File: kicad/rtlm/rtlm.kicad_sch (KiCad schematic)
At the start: 265 parts, among them IC1 ESP32-S3FN8, IC2 TPS25940ARVCR, IC3 PE4259, IC4 TPS2553DBVR, IC5 TLV9004IDR, IC6 TLV9004IDR, IC7 TCAN1042HGVDR, IC8 TPS2553DBVR, IC9 TLC59116IPWR, J1 USB_C_Receptacle_USB2.0_16P, J10 TEMP_2, J11 TEMP_3, J12 TEMP_4, J13 ANALOG_1, J14 ANALOG_2, J15 ANALOG_3, J16 ANALOG_4, J17 DM3AT-SF-PEJM5, J18 CAN_EXPANSION, J19 BATTERY_VOLTAGE_SENSE_LINE, J2 Conn_01x02, J3 UART_DEBUG_3V3, J4 LORA_ANT, J5 PULSE_1, J6 PULSE_2, J7 PULSE_3, J8 PULSE_4, J9 TEMP_1, Q1 DMP2035U-7, SW1 SW_Push, SW2 SW_Push, U1 TPS62130A, U10 RV-3028-C7, U2 TPS2116DRL, U3 TPD2EUSB30, U4 SX1262IMLTRT, U5 SN74LVC14ADR, U6 MCP3208-BI/SL, U7 REF3025AIDBZR, U8 AMC3330, U9 ADS1115IDGS, Y1 40MHz, Y2 TG2520SMN 32.0000M-MCGNNM3

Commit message: Separate USB programming power and protect the pack divider
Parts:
- added D35: BAS70-04, Package_TO_SOT_SMD:SOT-23, symbol Device:D_Schottky_Dual_Series_AKC
- added R95: 16.4k, Resistor_SMD:R_0603_1608Metric, symbol Device:R
- C4: value 3.3nf -> 22nF; MPN CC0603KRX7R9BB332 -> CC0603KRX7R9BB223; Selection Notes Specified MLCC value/package; manufacturer datasheet and DC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 -> Slower MCU-only buck soft start for USB programming inrush;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
- R84: value 8.2k -> 16.4k; MPN TNPW06038K20BEEA -> TNPW060316K4BEEA
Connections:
- net +3.3V: no longer C10.2, C11.2, C14.2, C15.2, C16.1, C3.1, IC1.20 (VDD3P3_RTC), IC1.46 (VDD3P3_CPU), IC1.55 (VDDA_1), IC1.56 (VDDA_2), L1.2, L2.1, R16.2, R17.2, R6.2, U1.14 (VOS)
- net HLDO_OUT: now also D35.2 (K)
- net PACK_NEG: now also D35.1 (A), R95.1
- net PACK_V_SENSE: now also D35.3 (common)
- net PACK_DIVIDED: now reaches C74.1, R83.2, R84.2, R90.1
- net PACK_DIVIDED: now also R95.2
- net MUX_EXT_SELECTED: now reaches R8.1, U2.8 (ST)
- new net +3V3_MCU: C10.2, C11.2, C14.2, C15.2, C16.1, C3.1, IC1.20 (VDD3P3_RTC), IC1.46 (VDD3P3_CPU), IC1.55 (VDDA_1), IC1.56 (VDDA_2), L1.2, L2.1, R16.2, R17.2, R6.2, U1.14 (VOS)
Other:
- added sheet USB service power (service_power.kicad_sch)
- note added: "R84 || R95 = 8.2k. One leg open at96V: INP <1.56V. D35: isolated-rail clamps."

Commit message: Move USB service-power circuit into the main schematic
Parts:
- added C82, C85, C88, C89: 100nF, Capacitor_SMD:C_0603_1608Metric, symbol Device:C
- added C83: 1uF, Capacitor_SMD:C_0603_1608Metric, symbol Device:C
- added C84: 1nF, Capacitor_SMD:C_0603_1608Metric, symbol Device:C
- added C86: 130pF, Capacitor_SMD:C_0603_1608Metric, symbol Device:C
- added C87: 220nF, Capacitor_SMD:C_0603_1608Metric, symbol Device:C
- added C90: 10nF, Capacitor_SMD:C_0603_1608Metric, symbol Device:C
- added Q2, Q3: MMBT3904-7-F, Package_TO_SOT_SMD:SOT-23, symbol Transistor_BJT:Q_NPN_BEC
- added R100: 100, Resistor_SMD:R_0603_1608Metric, symbol Device:R
- added R101, R103, R98: 10k, Resistor_SMD:R_0603_1608Metric, symbol Device:R
- added R102, R104, R105, R96: 100k, Resistor_SMD:R_0603_1608Metric, symbol Device:R
- added R97: 1M, Resistor_SMD:R_0603_1608Metric, symbol Device:R
- added R99: 47k, Resistor_SMD:R_0603_1608Metric, symbol Device:R
- added U11: TPS22917DBVR, Package_TO_SOT_SMD:SOT-23-6, symbol Power_Management:TPS22917DBV
- added U12: TPS3808G01DBVR, Package_TO_SOT_SMD:SOT-23-6, symbol Power_Supervisor:TPS3808DBV
- added U13: SN74LVC1G17DBVR, Package_TO_SOT_SMD:SOT-23-5, symbol 74xGxx:74LVC1G17
- added U14: SN74LVC2G86DCTR, Package_SO:SSOP-8_2.95x2.8mm_P0.65mm, symbol 74xGxx:74LVC2G86
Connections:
- net +3.3V: now also C83.1, R100.1, U11.6 (VOUT)
- net +3V3_MCU: now also C82.1, C84.2, C85.1, C88.1, C89.1, R98.1, U11.1 (VIN), U12.3 (~{MR}), U12.6 (VDD), U13.5 (VCC), U14.6, U14.8 (VCC)
- net ESP_BOOT: now also Q3.3 (C)
- net ESP_RESET: now also Q2.3 (C)
- net GND: now also C82.2, C83.2, C85.2, C86.2, C87.2, C88.2, C89.2, C90.2, Q2.2 (E), Q3.2 (E), R102.2, R104.2, R105.2, R97.2, U11.2 (GND), U12.2 (GND), U13.3 (GND), U14.4 (GND)
- net MUX_EXT_SELECTED: now also R96.1
- new net BOOT_BASE: Q3.1 (B), R103.2, R104.1
- new net EXT_SENSE: C90.1, R96.2, R97.1, U12.5 (SENSE)
- new net EXT_VALID: R98.2, R99.1, U12.1 (~{RESET}), U14.1, U14.5
- new net MODE_EDGE: R101.1, U14.7
- new net PERIPH_ENABLE: R105.1, U11.3 (ON), U13.4, U14.2
- new net PERIPH_QOD: R100.2, U11.5 (QOD)
- new net RESET_BASE: Q2.1 (B), R101.2, R102.1
- new net SERVICE_DELAY: C87.1, R99.2, U13.2
- new net SUPERVISOR_CT: C86.1, U12.4 (CT)
- new net SWITCH_CT: C84.1, U11.4 (CT)
- new net USB_SERVICE: R103.1, U14.3
- no-connect marks 44 -> 45
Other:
- removed sheet USB service power
- note added: "Automatic USB programming service mode"
- note added: "TPS22917 CT -> VIN. Reset pulse = raw flag XOR Schmitt-delayed flag. Q2/Q3 are open collector; manual BOOT and RESET remain usable. Do not disable ROM USB download with security eFuses if USB service is required."
- note added: "USB only: peripherals OFF; GPIO0 forced LOW; ESP boots ROM download. Mux confirms external5V selected: peripherals ramp ON; ESP resets and boots application. Either power-mode transition resets ESP before peripheral power changes."

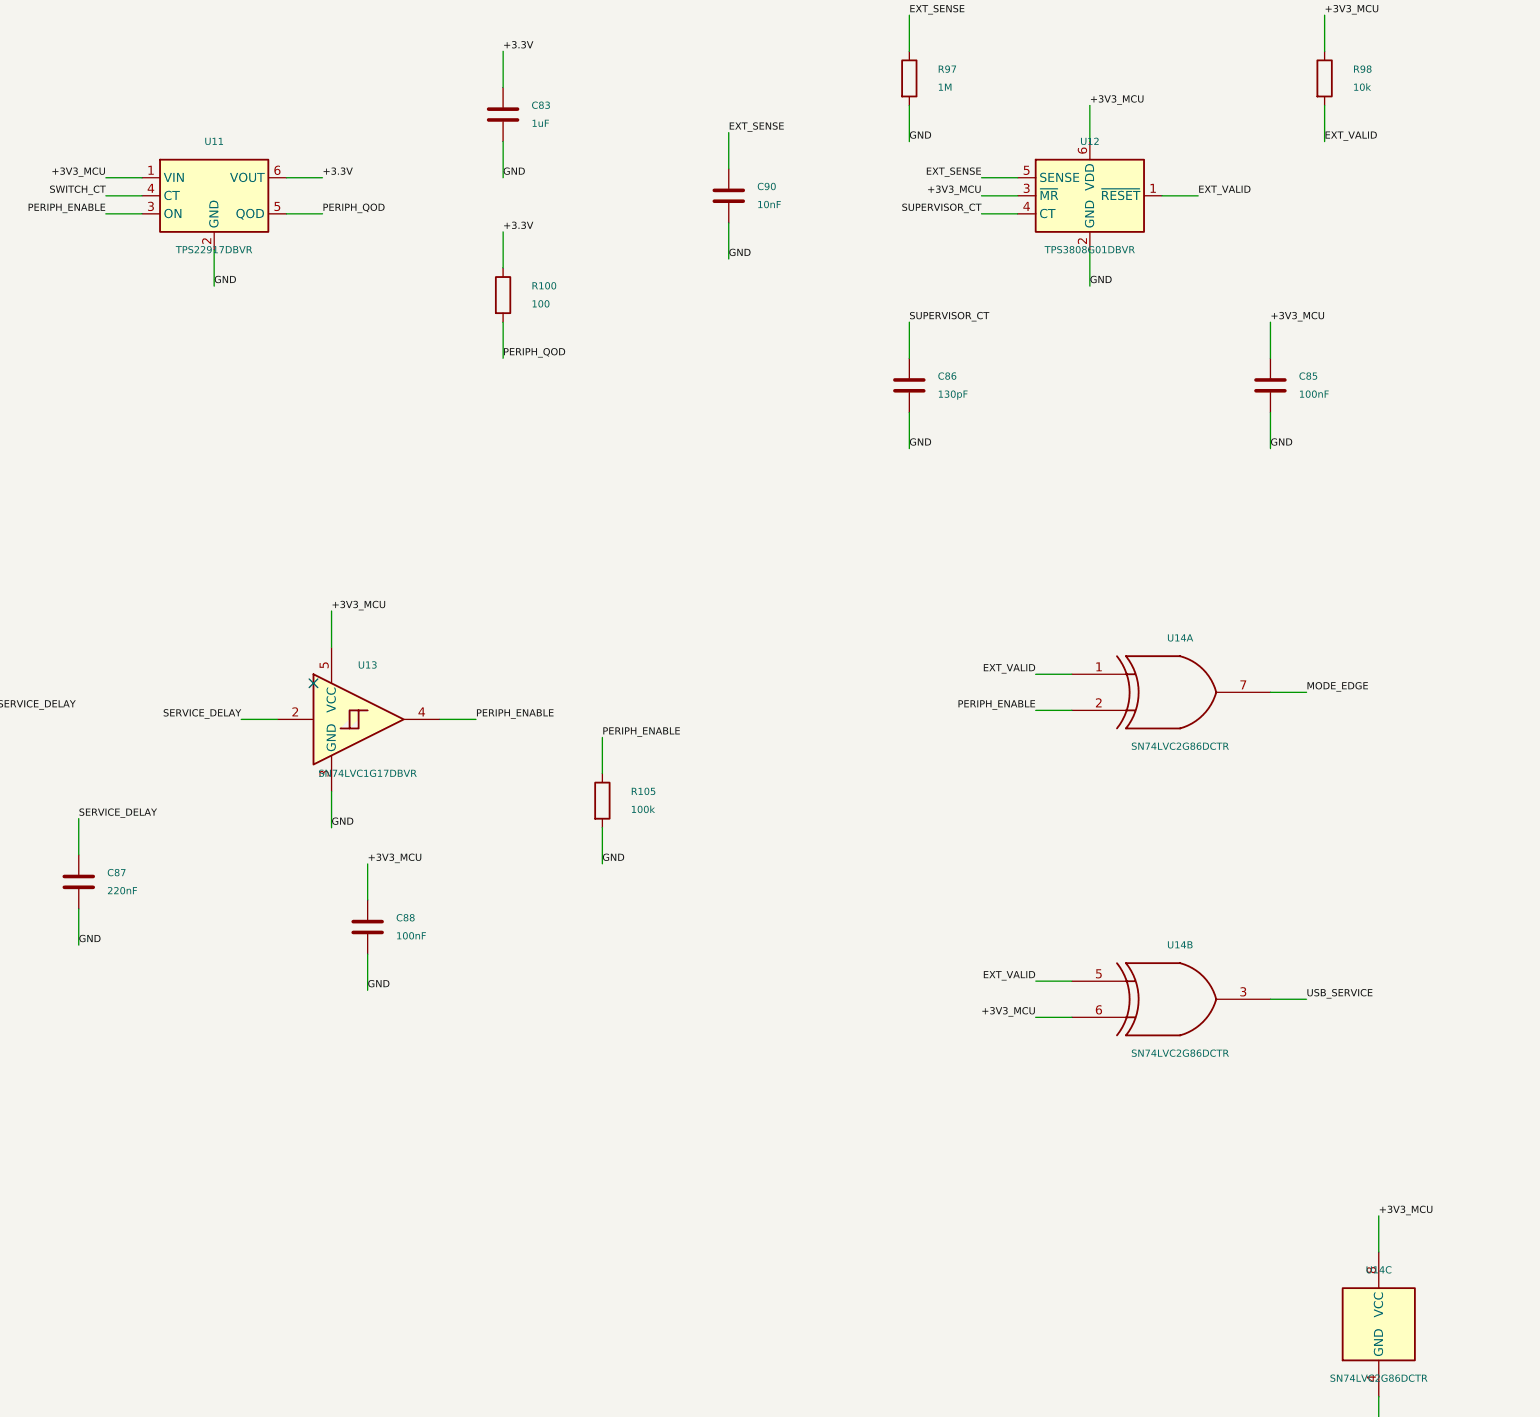
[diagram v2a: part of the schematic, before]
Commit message: Balance USB-C routing and condition service-power logic
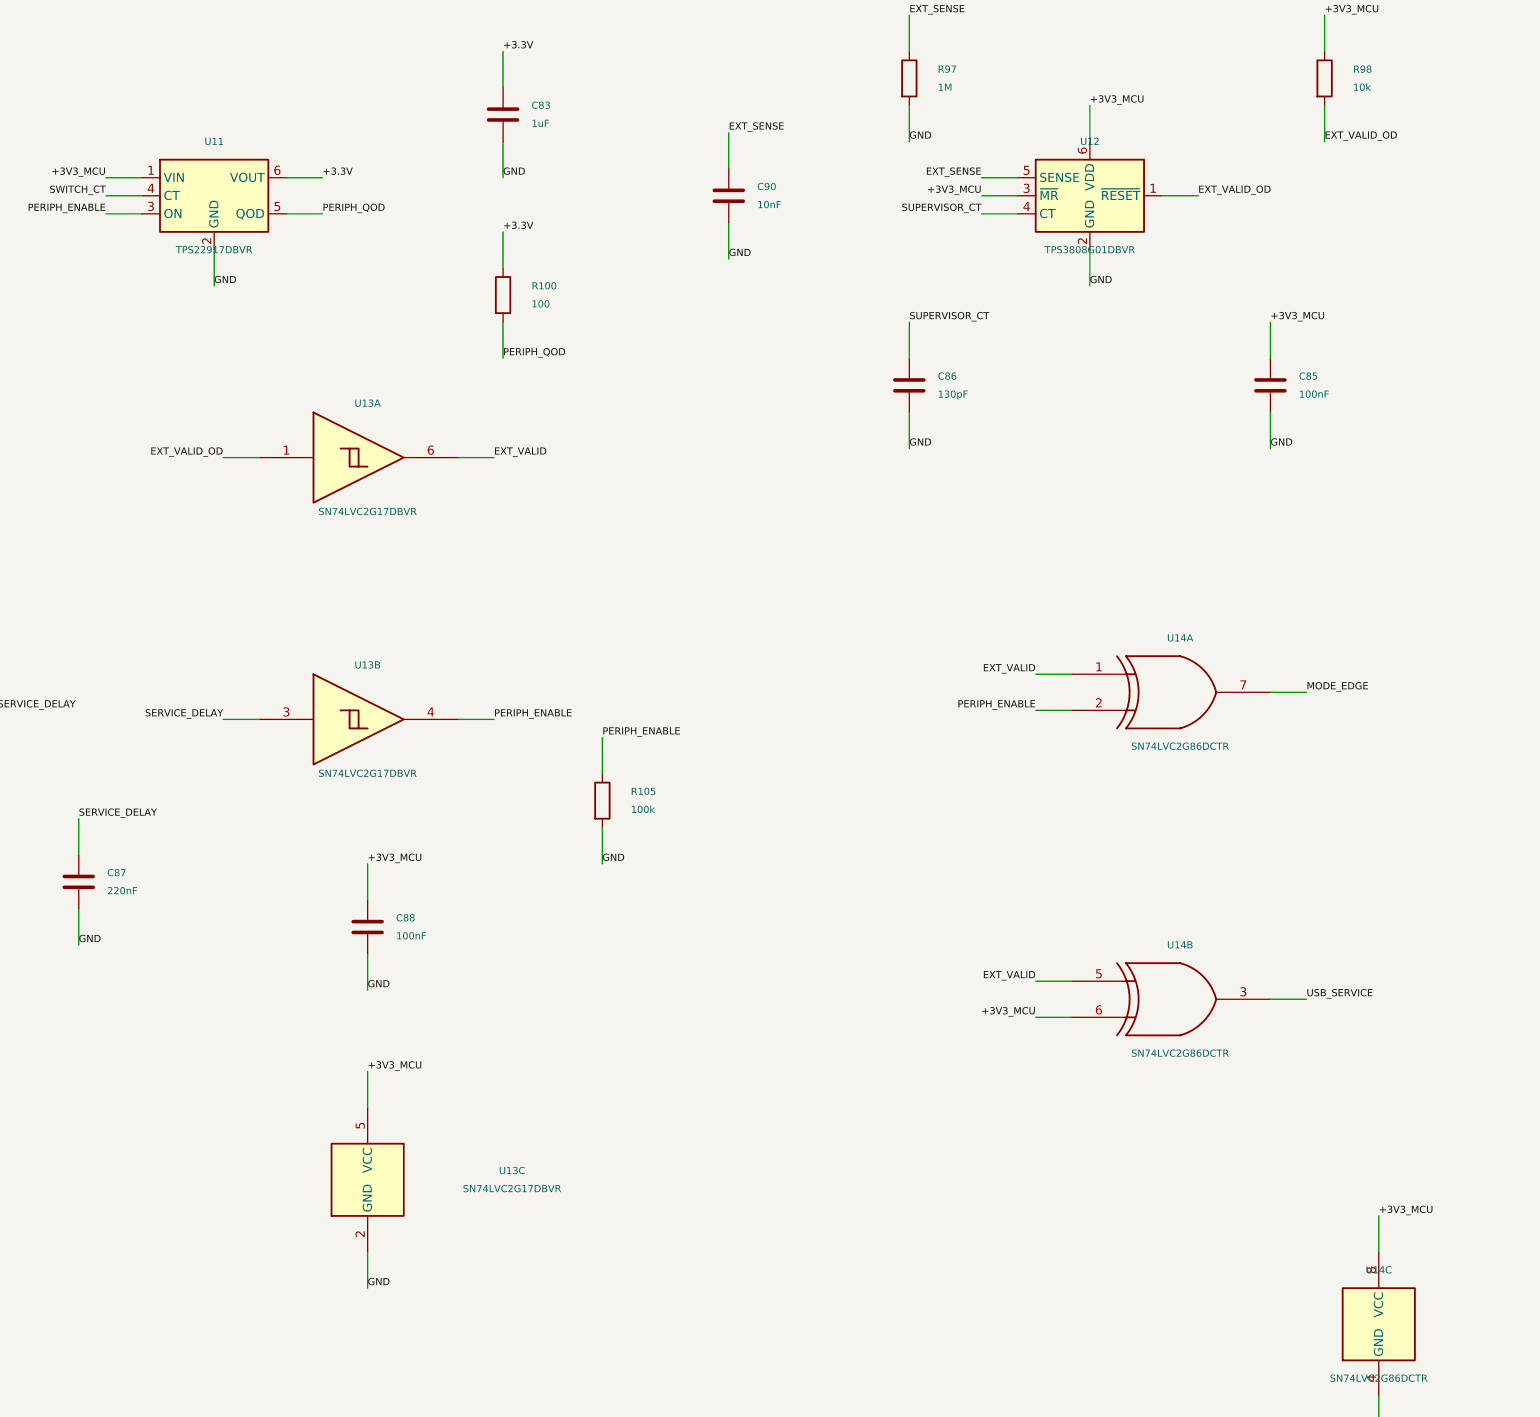
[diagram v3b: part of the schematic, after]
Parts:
- added unit 2 of U13
- added unit 3 of U13
- U13: value SN74LVC1G17DBVR -> SN74LVC2G17DBVR; footprint Package_TO_SOT_SMD:SOT-23-5 -> Package_TO_SOT_SMD:SOT-23-6; symbol 74xGxx:74LVC1G17 -> 74xGxx:74LVC2G17; LCSC Part Number (none) -> C10429; MPN SN74LVC1G17DBVR -> SN74LVC2G17DBVR; Selection Notes Schmitt buffer makes RC transition logic-safe. Delayed flag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 -> Dual Schmitt buffer: A cleans TPS3808 open-drain raw flag b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
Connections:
- net +3V3_MCU: now also U13.5 (VCC); no longer U13.5 (VCC)
- net EXT_VALID: now also U13.6; no longer R98.2, U12.1 (~{RESET})
- net GND: now also U13.2 (GND); no longer U13.3 (GND)
- net PERIPH_ENABLE: now also U13.4; no longer U13.4
- net SERVICE_DELAY: now also U13.3; no longer U13.2
- net EXT_VALID_OD: now reaches U13.1
- net EXT_VALID_OD: now also R98.2, U12.1 (~{RESET})
- no-connect marks 45 -> 44

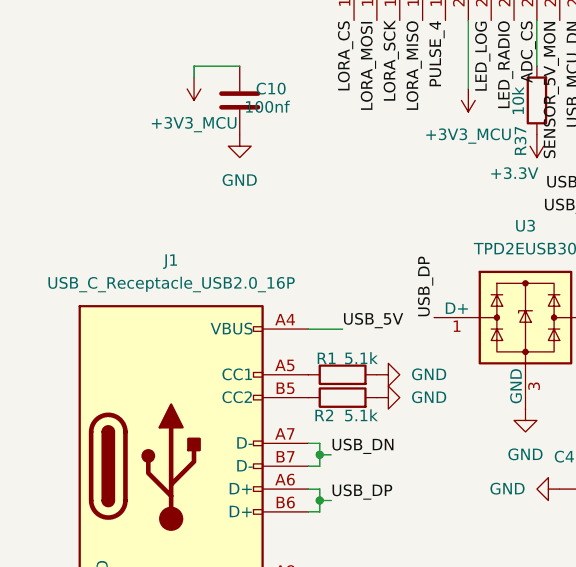
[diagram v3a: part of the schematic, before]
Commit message: Replace USB receptacle with verified HRO manufacturer land pattern
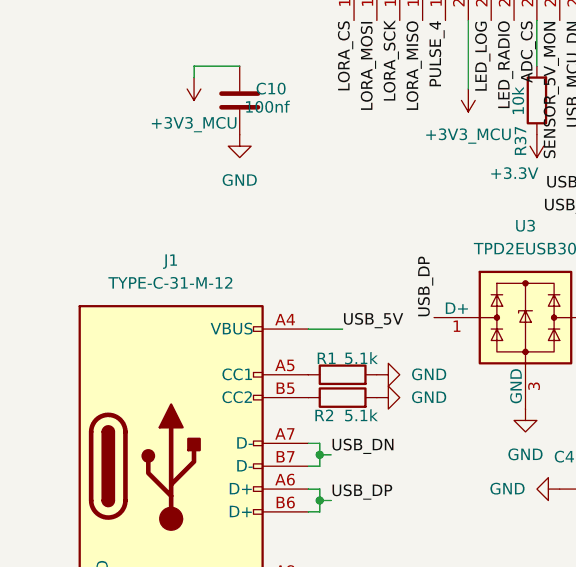
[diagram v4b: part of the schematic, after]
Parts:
- J1: value USB_C_Receptacle_USB2.0_16P -> TYPE-C-31-M-12; footprint RTLM_Local:USB_C_GCT_USB4105_JLC_NPTH_Clearance -> RTLM_Local:USB_C_HRO_TYPE_C_31_M_12_OEM_20201208; LCSC Part Number (none) -> C165948; MPN USB4105-GF-A -> TYPE-C-31-M-12; Manufacturer GCT -> Korean Hroparts Elec; Selection Notes USB4105 top-mount USB2 Type-C; verify selected staking leng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 -> HRO current2020-12-08 recommended land pattern, full lands 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
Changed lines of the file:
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@@
 			)
 		)
-		(property "Value" "USB_C_Receptacle_USB2.0_16P"
+		(property "Value" "TYPE-C-31-M-12"
 			(at 29.21 147.32 0)
 			(show_name no)
@@
 			)
 		)
-		(property "Footprint" "RTLM_Local:USB_C_GCT_USB4105_JLC_NPTH_Clearance"
+		(property "Footprint" "RTLM_Local:USB_C_HRO_TYPE_C_31_M_12_OEM_20201208"
 			(at 33.02 167.64 0)
 			(hide yes)
@@
 			)
 		)
-		(property "Datasheet" "https://gct.co/files/drawings/usb4105.pdf"
+		(property "Datasheet" "https://www.lcsc.com/datasheet/C165948.pdf"
 			(at 33.02 167.64 0)
 			(hide yes)
@@
 			)
 		)
-		(property "Manufacturer" "GCT" (at 0 0 0) (hide yes) (effects (font (size 1.27 1.27))))
-		(property "MPN" "USB4105-GF-A" (at 0 0 0) (hide yes) (effects (font (size 1.27 1.27))))
-		(property "Selection Notes" "USB4105 top-mount USB2 Type-C; verify selected staking length against board/case." (at 0 0 0) (hide yes) (effects (font (size 1.27 1.27))))
+		(property "Manufacturer" "Korean Hroparts Elec" (at 0 0 0) (hide yes) (effects (font (size 1.27 1.27))))
+		(property "MPN" "TYPE-C-31-M-12" (at 0 0 0) (hide yes) (effects (font (size 1.27 1.27))))
+		(property "Selection Notes" "HRO current2020-12-08 recommended land pattern, full lands and0.60mm locating holes. USB4105 is NOT a compatible substitute. JLC local0.20mm NPTH-to-land rule. See fabrication notes." (at 0 0 0) (hide yes) (effects (font (size 1.27 1.27))))
 		(pin "B5"
 		)
@@
 			)
 		)
-	)
+	(property "LCSC Part Number" "C165948" (at 0 0 0) (hide yes) (effects(font(size 1 1)))))
 	(symbol
 		(lib_id "Device:R")
